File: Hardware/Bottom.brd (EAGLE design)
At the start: 120 x 80 mm, 13 parts, among them IC1 SI570, IC2 74LVC74A, X1 MINI-USB-SCHIELD-32005-201

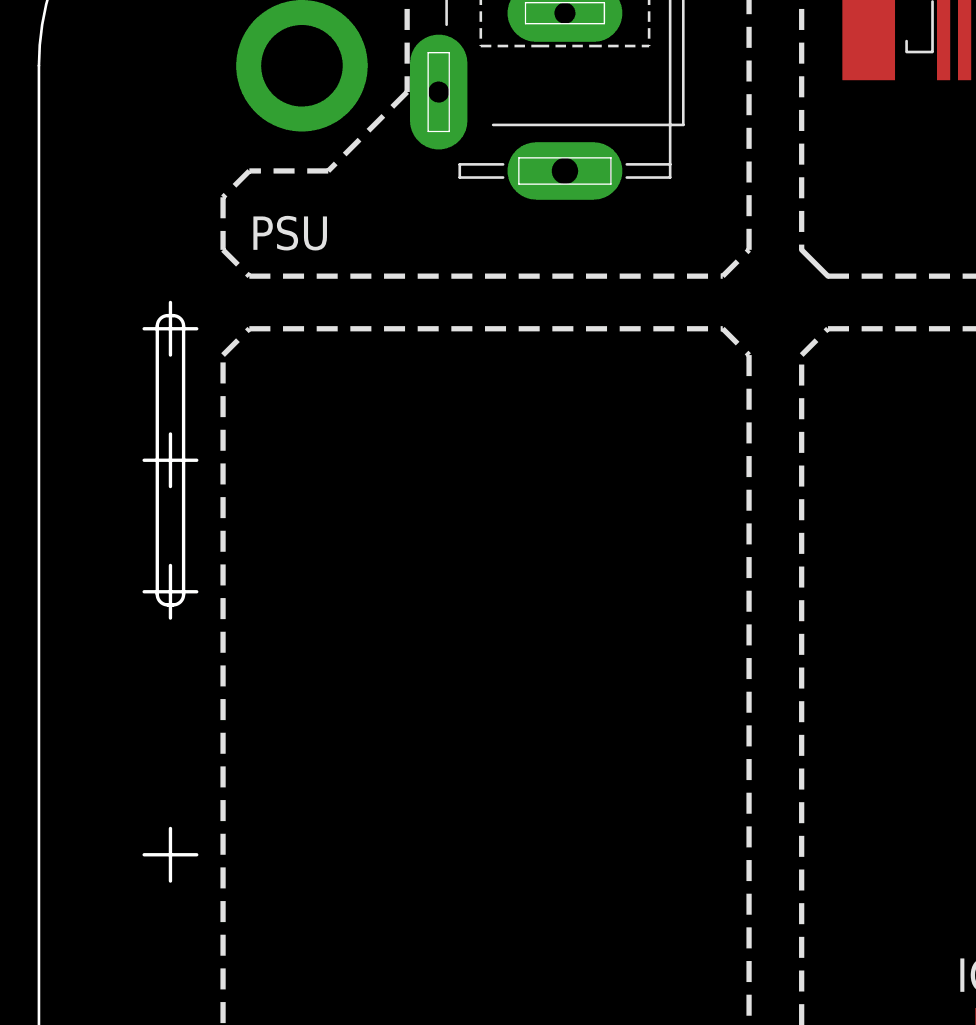
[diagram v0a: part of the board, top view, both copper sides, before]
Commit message: Add stepdown converters
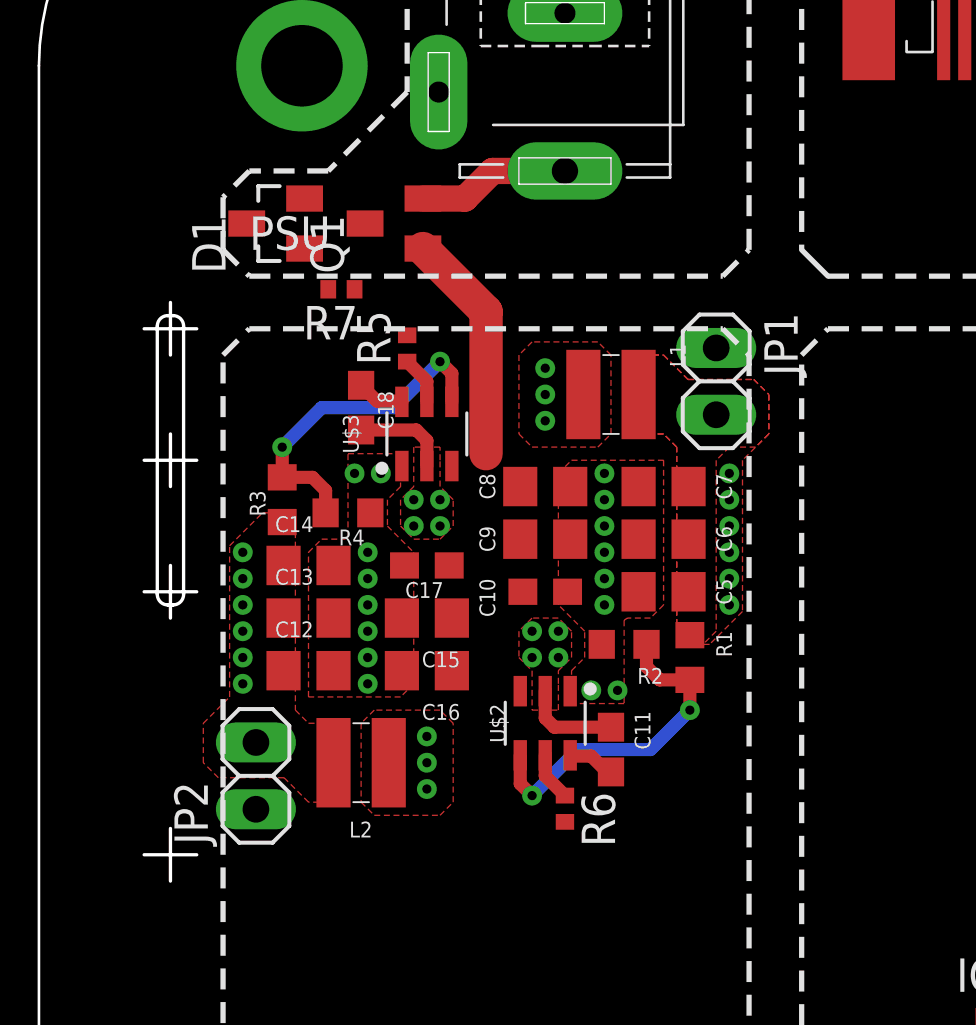
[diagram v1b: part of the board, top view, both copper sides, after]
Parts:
- added C10, C11, C17, C18: 100n, rcl:C0603
- added C12, C13, C14, C5, C6, C7: 22µ, rcl:C0805
- added C15, C16, C8, C9: 10µ, rcl:C0805
- added D1: 10V, diode:SOT23
- added JP1, JP2: (no value), pinhead:1X02
- added L1, L2: 4.7µH, PowerMagnetics (rev18d):WE-MAPI_3015/3020
- added Q1: DMPH6050SK3, MyLib:SOT23
- added R1: 54k9, rcl:R0603
- added R2, R4: 10k, rcl:R0603
- added R3: 33k2, rcl:R0603
- added R5, R6: 10k, rcl:R0402
- added R7: 100k, rcl:R0402
- added U$2, U$3: TPS562201, MyLib:SOT95P280X110-6
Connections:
- new net +5V: JP1.1
- new net N$10: D1.3, Q1.3
- new net N$11: R1.2, R2.2, U$2.4
- new net N$12: J1.3, Q1.2
- new net N$15: C18.1, U$3.6
- new net N$19: C18.2, L2.1, U$3.2
- new net N$20: R3.2, R4.2, U$3.4
- new net N$30: C5.1, C6.1, C7.1, JP1.2, L1.2, R1.1
- new net N$31: C12.1, C13.1, C14.1, JP2.2, L2.2, R3.1
- new net N$7: C11.1, U$2.6
- new net N$8: C11.2, L1.1, U$2.2
- new net N$9: D1.1, Q1.1, R7.2
- new net VDDDC: C10.1, C15.1, C16.1, C17.1, C8.1, C9.1, R5.2, R6.2, U$2.3, U$3.3
- new net VREG_VDD3V3_EN: R5.1, U$3.5
- new net VREG_VDD5_EN: R6.1, U$2.5
- net +3V3: now also JP2.1
- net GND: now also C10.2, C12.2, C13.2, C14.2, C15.2, C16.2, C17.2, C5.2, C6.2, C7.2, C8.2, C9.2, J1.1, R2.1, R4.1, R7.1, U$2.1, U$3.1
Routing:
- net N$20: track 0.00 -> 12.9 mm, vias 0 -> 2
- net N$11: track 0.00 -> 12.9 mm, vias 0 -> 2
- net N$9: track 0.00 -> 8.79 mm
- net N$12: track 0.00 -> 5.83 mm
- net N$8: track 0.00 -> 3.67 mm, vias 0 -> 7
- net N$19: track 0.00 -> 3.64 mm, vias 0 -> 7
- net VREG_VDD5_EN: track 0.00 -> 1.84 mm
- net VREG_VDD3V3_EN: track 0.00 -> 1.84 mm
- net N$15: track 0.00 -> 1.81 mm
- net N$7: track 0.00 -> 1.81 mm
- added copper zone on layer 1, net GND
- added copper zone on layer 1, net N$19
- added copper zone on layer 2, net N$19
- added copper zone on layer 1, net N$30
- added copper zone on layer 1, net N$31
- added copper zone on layer 1, net N$8
- added copper zone on layer 2, net N$8

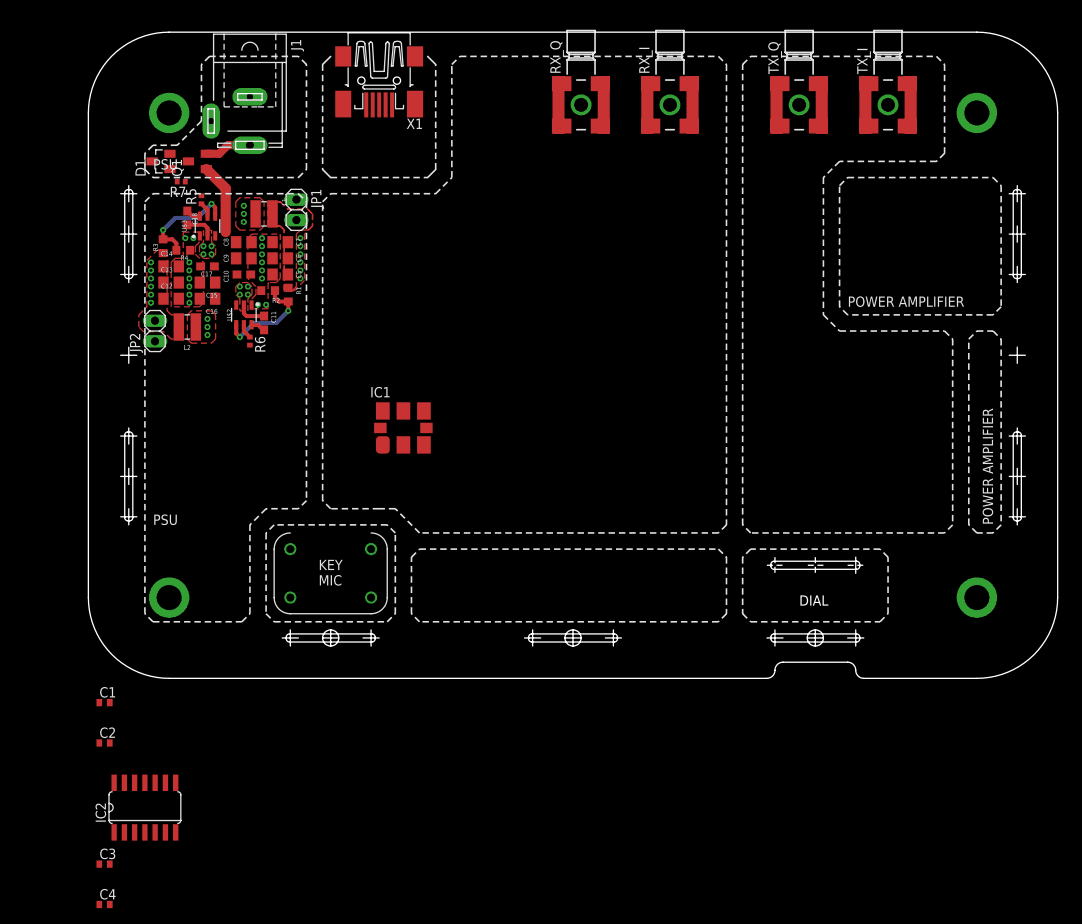
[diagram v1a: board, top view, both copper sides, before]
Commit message: Add sides, add Tayloe Detector
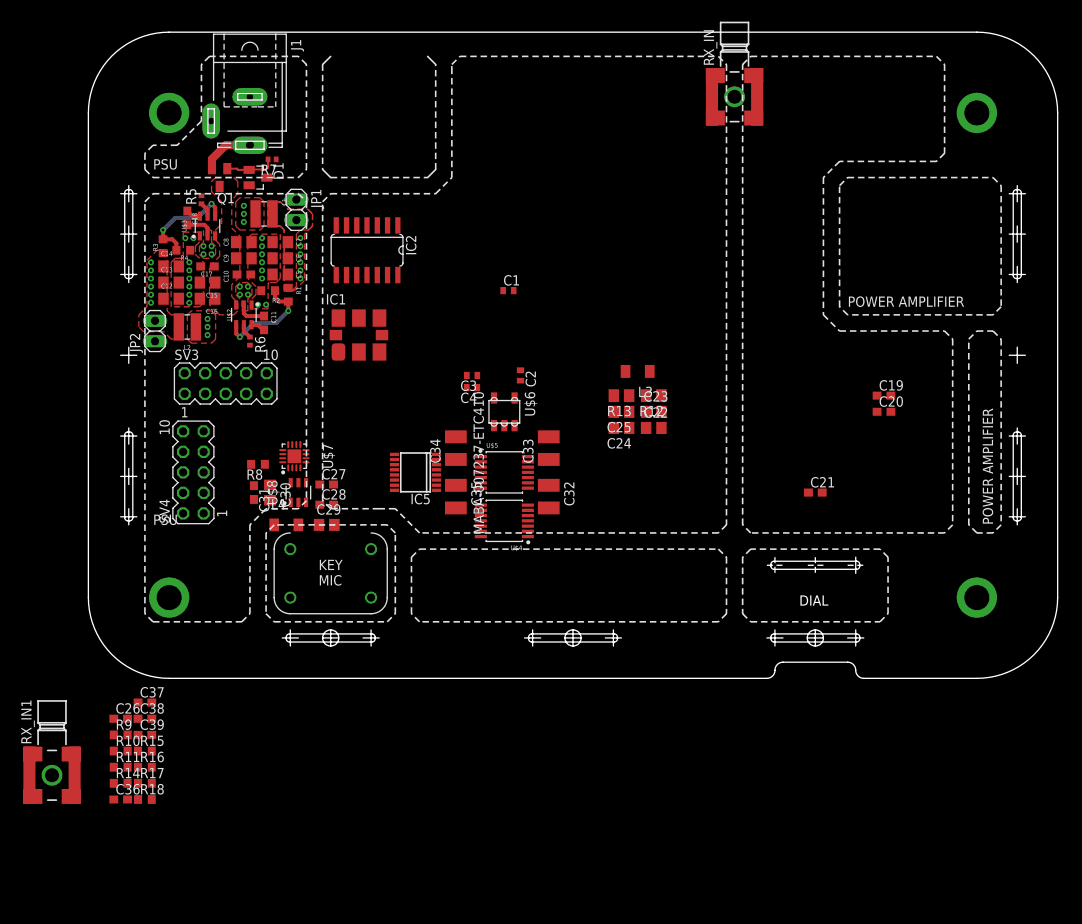
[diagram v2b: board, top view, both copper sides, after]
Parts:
- removed RX_I, RX_Q, TX_I, TX_Q: PE44121, con-coax:PE44121
- removed X1: MINI-USB-SCHIELD-32005-201, con-cypressindustries:32005-201
- added C19, C20, C21, C26, C27, C31: 100n, rcl:C0603
- added C22, C23, C24, C25: 4µ7, rcl:C0805
- added C28: 1µ, rcl:C0603
- added C29, C30: 2µ, rcl:C0805
- added C32, C33, C34, C35: (no value), rcl:C1210
- added C36, C37, C38, C39: (no value), rcl:C0603
- added IC5: LT6232CGN, linear-technology:SSOP16
- added L3, L4: 33µ, rcl:L3216C
- added R10, R11, R14, R15, R16, R17, R18, R9: (no value), rcl:R0603
- added R12, R13: 10k, rcl:M0805
- added R8: 10k, rcl:R0603
- added RX_IN, RX_IN1: PE44121, con-coax:PE44121
- added SV3, SV4: (no value), con-lstb:MA05-2
- added U$4, U$5: TMUX1511TSSOP14, MyLib:SOP65P650X120-14
- added U$6: MABA-007237-ETC410, MyLib:MABA-007237-ETC410
- added U$7: ADS7946, MyLib:QFN50P300X300X80-17T170
- added U$8: MCP1501, MyLib:SOT95P280X110-6
- moved C4 78.5 mm to (47.5, 36.0), turned to 180 degrees
- moved C3 75.7 mm to (47.5, 37.5), turned to 180 degrees
- moved IC2 74.3 mm to (34.5, 53.0), turned to 180 degrees
- moved C1 71.4 mm to (52.0, 48.0)
- moved C2 68.7 mm to (53.5, 37.5), turned to 270 degrees
- moved IC1 12.7 mm to (33.5, 42.5)
- moved D1 12.2 mm to (21.0, 62.0), turned to 270 degrees
- moved R7 11.6 mm to (22.8, 64.2)
- moved Q1 3.40 mm to (16.2, 62.0), turned to 180 degrees
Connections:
- net DDS_SCL renamed I2C_OSC_SCL
- net DDS_SDA renamed I2C_OSC_SDA
- removed net DDS_OE: IC1.2
- removed net VDDDC: C10.1, C15.1, C16.1, C17.1, C8.1, C9.1, R5.2, R6.2, U$2.3, U$3.3
- new net ADC_CHSEL: SV4.1, U$7.11
- new net I2C_MCS_SCL: SV3.9
- new net I2C_MCS_SDA: SV3.10
- new net N$13: C37.1, IC5.14, R14.2
- new net N$14: IC5.1, R9.1
- new net N$16: C21.1, RX_IN.1
- new net N$17: C21.2, U$6.PD
- new net N$18: C22.1, C23.1, C24.1, C25.1, L3.1, R12.2, U$6.CT
- new net N$21: L3.2, R13.1
- new net N$22: U$4.11, U$4.3, U$4.6, U$4.8, U$6.SD
- new net N$23: U$5.11, U$5.3, U$5.6, U$5.8, U$6.S
- new net N$24: C32.1, IC5.3, U$4.2, U$5.9
- new net N$25: U$7.8
- new net N$26: U$7.7
- new net N$27: U$7.3, U$8.1
- new net N$28: U$7.6
- new net N$29: C27.1, C28.1, C29.1, L4.2, U$7.2, U$8.4, U$8.6
- new net N$32: U$7.5
- new net N$33: C33.1, IC5.5, U$4.5, U$5.12
- new net N$34: C34.1, IC5.2, U$4.9, U$5.2
- new net N$35: SV4.10
- new net N$36: SV4.8
- new net N$37: SV4.6
- new net N$38: SV4.4
- new net N$39: C35.1, IC5.6, U$4.12, U$5.5
- new net N$40: C38.1, R10.1, R9.2
- new net N$41: C36.1, IC5.12, R10.2
- new net N$42: C38.2, IC5.10, R18.1
- new net N$43: C39.2, IC5.16, R16.1
- new net N$44: IC5.15, R15.2, R16.2
- new net N$45: IC5.11, R17.2, R18.2
- new net N$6: IC5.7, R11.1
- new net RESV_NC: SV4.2
- new net SPI_ADC_MISO: R8.1, U$7.15
- new net SPI_MCS_CLK: SV4.9, U$7.14
- new net SPI_MCS_CS: SV4.3, U$7.13
- new net SPI_MCS_MISO: R8.2, SV4.5
- new net SPI_MCS_MOSI: SV4.7
- new net VDD_DC: C10.1, C15.1, C16.1, C17.1, C8.1, C9.1, D1.3, Q1.3, R5.2, R6.2, U$2.3, U$3.3
- net +3V3: now also C19.1, C20.1, C30.1, C31.1, R13.2, SV3.6, SV3.8, U$4.14, U$5.14, U$7.16
- net +5V: now also C26.1, IC5.4, SV3.2, SV3.4
- net GND: now also C19.2, C20.2, C22.2, C23.2, C24.2, C25.2, C26.2, C27.2, C28.2, C29.2, C30.2, C31.2, C32.2, C33.2, C34.2, C35.2, C36.2, C37.2, IC5.13, R12.1, R15.1, R17.1, RX_IN.2@1, RX_IN.2@2, RX_IN.2@3, RX_IN.2@4, RX_IN.2@5, RX_IN.2@6, RX_IN1.2@1, RX_IN1.2@2, RX_IN1.2@3, RX_IN1.2@4, RX_IN1.2@5, RX_IN1.2@6, SV3.1, SV3.3, SV3.5, SV3.7, U$4.7, U$5.7, U$6.P, U$7.1, U$7.10, U$7.12, U$7.17, U$7.4, U$7.9, U$8.2, U$8.3, U$8.5
- net N$10: now also C39.1, R11.2, R14.1; no longer D1.3, Q1.3
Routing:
- net N$9: track 8.79 -> 6.24 mm
- net N$12: track 5.83 -> 6.60 mm
- added copper zone on layer 1, net VDD_DC

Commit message: Adds SN74CBT3253 to Bottom
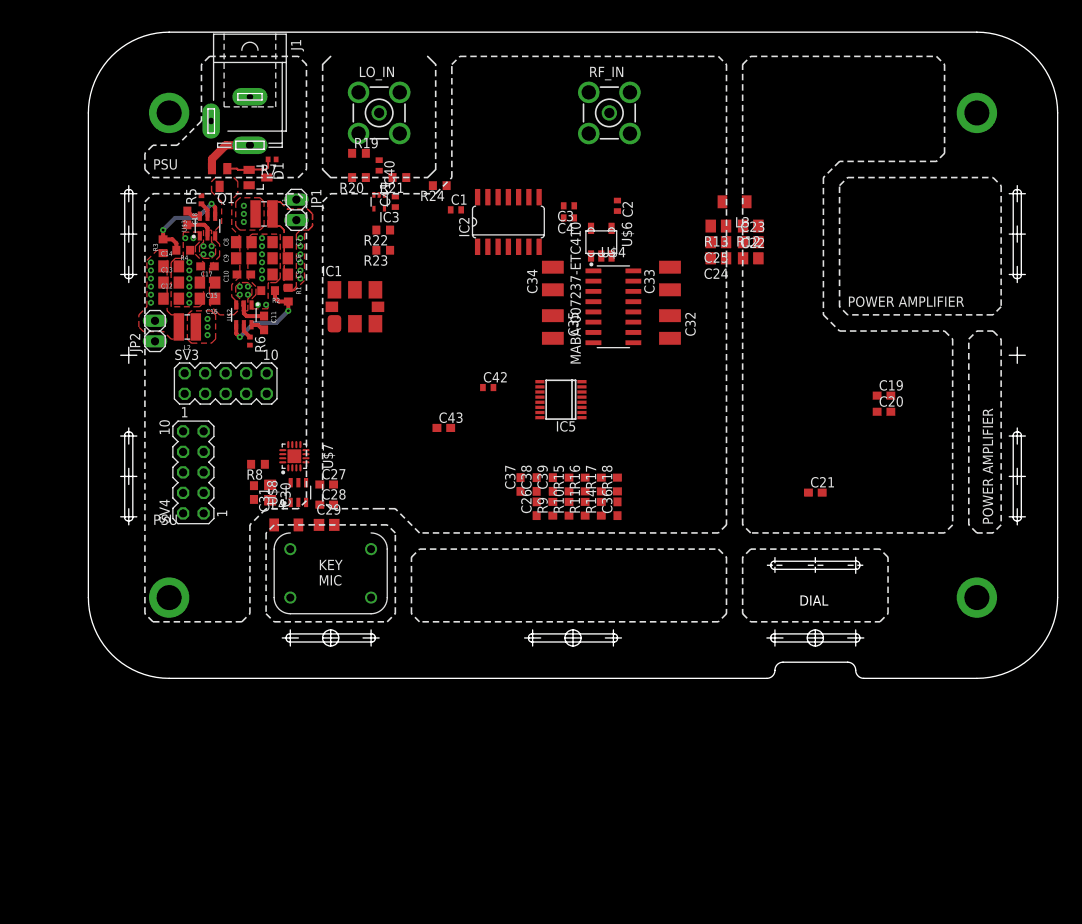
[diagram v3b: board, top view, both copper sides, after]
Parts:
- removed RX_IN, RX_IN1: PE44121, con-coax:PE44121
- removed U$5: TMUX1511TSSOP14, MyLib:SOP65P650X120-14
- added C40, C41: 100n, rcl:C0402
- added C42: 10n, rcl:C0402
- added C43: 1u, rcl:C0603
- added IC3: 74LVC1G17DCK, 74xx-little-de:SC70-5
- added LO_IN, RF_IN: BU-SMA-V, con-coax:BU-SMA-V
- added R19: 47R, rcl:R0603
- added R20, R21: 10k, rcl:R0603
- added R22, R23, R24: DNP, rcl:R0603
- U$4: value TMUX1511TSSOP14 -> SN74CBT3253SOIC16; device MyLib:SOP65P650X120-14 -> MyLib:SOIC127P600X175-16
- moved C36 71.3 mm to (65.5, 21.0), turned to 90 degrees
- moved R18 70.3 mm to (65.5, 24.0), turned to 90 degrees
- moved R14 68.5 mm to (63.5, 21.0), turned to 90 degrees
- moved R17 67.5 mm to (63.5, 24.0), turned to 90 degrees
- moved R11 65.8 mm to (61.5, 21.0), turned to 90 degrees
- moved R16 64.8 mm to (61.5, 24.0), turned to 90 degrees
- moved R10 63.1 mm to (59.5, 21.0), turned to 90 degrees
- moved R15 62.0 mm to (59.5, 24.0), turned to 90 degrees
- moved R9 60.4 mm to (57.5, 21.0), turned to 90 degrees
- moved C39 59.3 mm to (57.5, 24.0), turned to 90 degrees
- moved C26 57.7 mm to (55.5, 21.0), turned to 90 degrees
- moved C38 56.5 mm to (55.5, 24.0), turned to 90 degrees
- moved C37 53.8 mm to (53.5, 24.0), turned to 90 degrees
- moved U$4 29.7 mm to (65.0, 46.0), turned to 0 degrees
- moved C32 25.8 mm to (72.0, 43.5)
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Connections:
- removed net N$34: C34.1, IC5.2, U$4.9, U$5.2
- new net N$46: C40.1, LO_IN.1, R19.2
- new net N$47: C40.2, IC3.2, R20.1, R21.2, R24.2
- new net N$48: IC3.4, R22.2
- new net N$49: C15.1
- new net N$50: IC1.4, R23.2
- new net N$55: U$4.7, U$6.SD
- new net N$56: U$4.9, U$6.S
- new net N$59: C34.1, IC5.2, U$4.10, U$4.4
- new net V+: U$4.16
- new net V-: U$4.8
- net +3V3: now also C41.1, C42.1, IC3.5, R20.2; no longer SV3.6, SV3.8, U$4.14, U$5.14
- net +5V: now also C43.1
- net GND: now also C41.2, C42.2, C43.2, IC3.3, LO_IN.2, LO_IN.3, LO_IN.4, LO_IN.5, R19.1, R21.1, R24.1, RF_IN.2, RF_IN.3, RF_IN.4, RF_IN.5, U$4.1, U$4.15; no longer RX_IN.2@1, RX_IN.2@2, RX_IN.2@3, RX_IN.2@4, RX_IN.2@5, RX_IN.2@6, RX_IN1.2@1, RX_IN1.2@2, RX_IN1.2@3, RX_IN1.2@4, RX_IN1.2@5, RX_IN1.2@6, U$4.7, U$5.7
- net N$16: now also RF_IN.1; no longer RX_IN.1
- net N$2: now also R22.1, R23.1; no longer IC1.4
- net N$22: now also U$4.2; no longer U$4.11, U$4.3, U$4.6, U$4.8, U$6.SD
- net N$23: now also U$4.14; no longer U$5.11, U$5.3, U$5.6, U$5.8, U$6.S
- net N$24: now also U$4.12, U$4.6; no longer U$4.2, U$5.9
- net N$33: now also U$4.13; no longer U$5.12
- net N$39: now also U$4.11, U$4.3; no longer U$4.12, U$5.5
- net VDD_DC: no longer C15.1
